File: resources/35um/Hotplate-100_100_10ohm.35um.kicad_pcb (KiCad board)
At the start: 2 copper layers, 100 x 100 mm, 7 parts, among them J1 Hotplate_Power_Connection, J2 Hotplate_Power_Connection

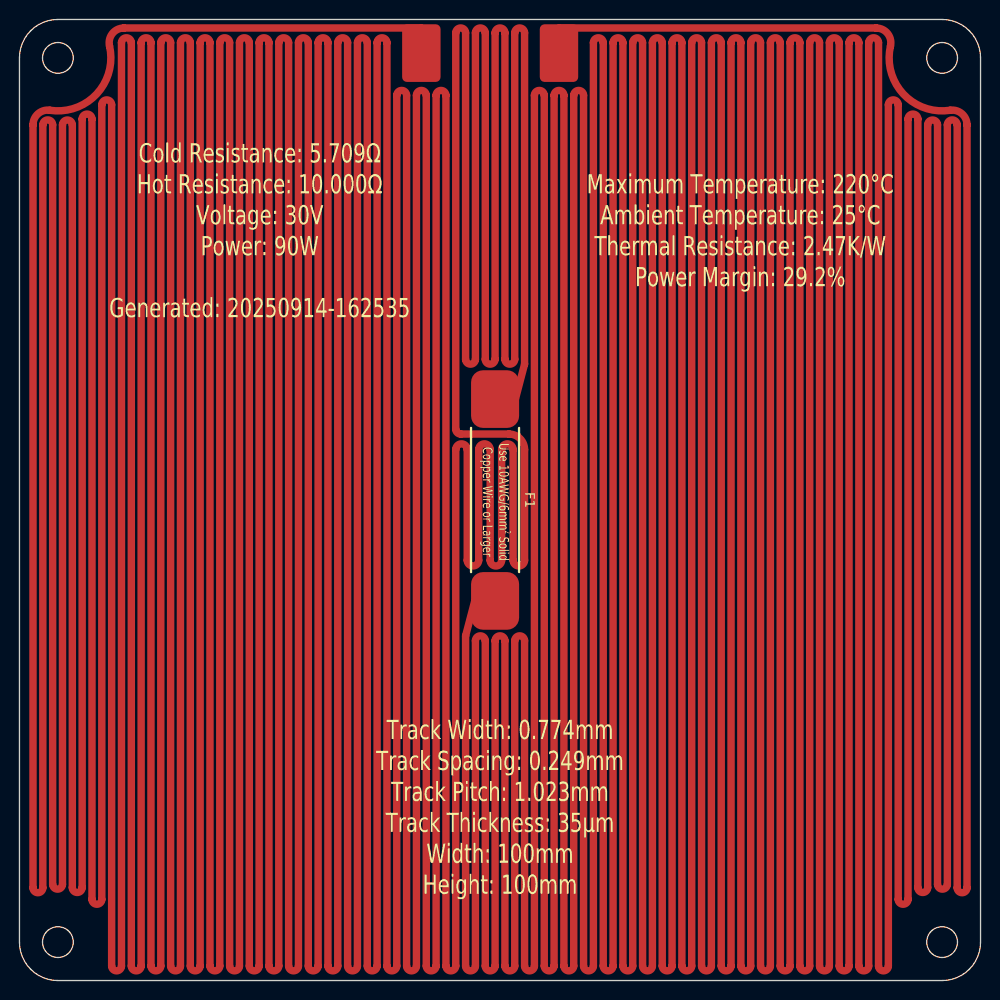
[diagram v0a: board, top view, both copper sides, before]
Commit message: Replaced obsolete 25mm thermal fuse footprint with new 35mm thermal fuse footprint.
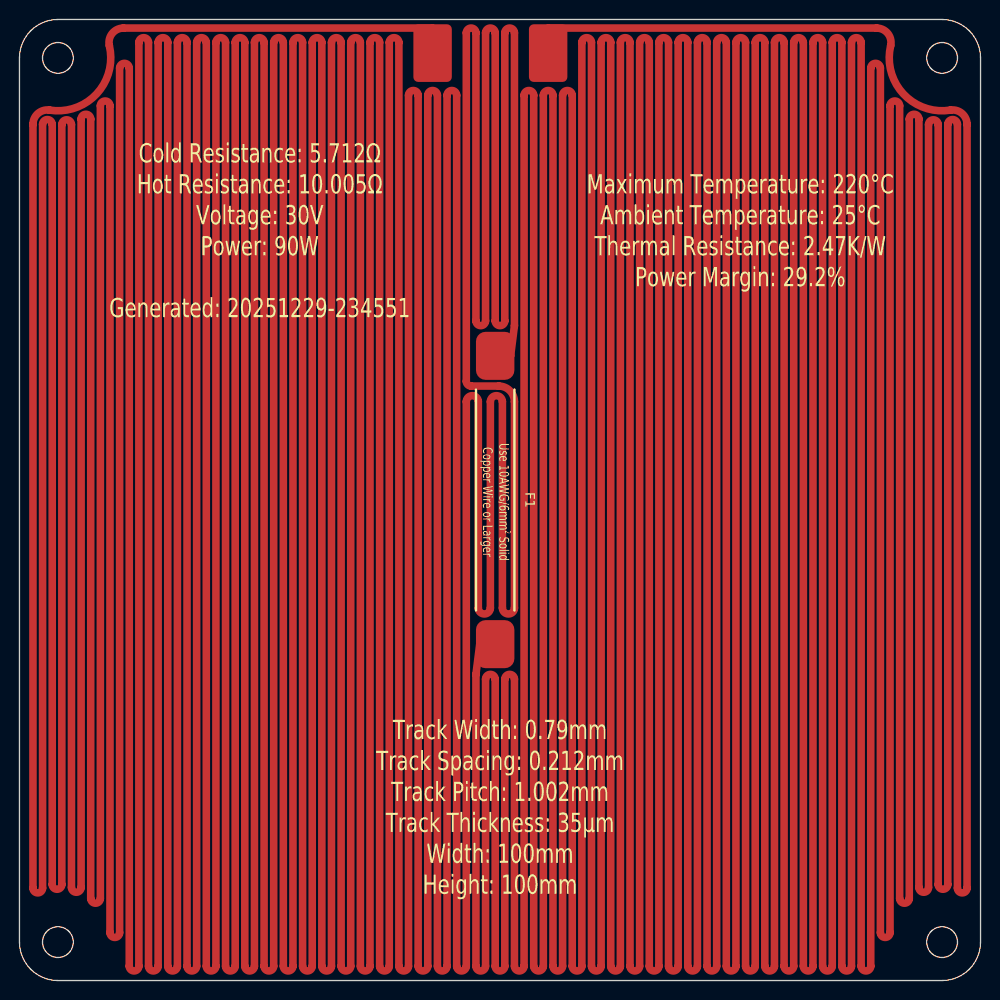
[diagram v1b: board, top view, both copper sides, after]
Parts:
- F1: footprint blg:Thermal Fuse, Front, 25mm -> blg:Thermal Fuse, SN100C, Front, 35mm
- moved J1 1.17 mm to (98.0, 58.5)
- moved J2 1.13 mm to (110.0, 58.5)
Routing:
- net Net-(J1-Pin_1): track 4510.5 -> 4613.9 mm
- net Net-(J2-Pin_1): track 4522.8 -> 4615.0 mm
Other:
- board text added: "Cold Resistance: 5.712Ω Hot Resistance: 10.005Ω Voltage: 30V Power: 90W Generated: 20251229-234551"
- board text added: "Track Width: 0.79mm Track Spacing: 0.212mm Track Pitch: 1.002mm Track Thickness: 35µm Width: 100mm Height: 100mm"
- board text removed: "Cold Resistance: 5.709Ω Hot Resistance: 10.000Ω Voltage: 30V Power: 90W Generated: 20250914-162535"
- board text removed: "Track Width: 0.774mm Track Spacing: 0.249mm Track Pitch: 1.023mm Track Thickness: 35µm Width: 100mm Height: 100mm"
